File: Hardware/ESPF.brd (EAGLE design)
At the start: 30 x 22 mm, 25 parts, among them IC1 CP2102N-A01-GQFN24, J1 USB-C-16P-16P, J2 ESPFLASH-1X6-2.54-PINS-RA, Q1 MMDT3904

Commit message: Wurth_Connectors_WR-USB
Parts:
- added J3: 629722000214, Wurth_Connectors_WR-USB:629722000214
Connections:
- removed net VIN: F1.1, J1.A4B9, J1.A9B4
- new net +5V: J3.A4, J3.A9, J3.B4, J3.B9
- net 5V: now also F1.1, J1.A4B9, J1.A9B4
- net D+: now also J3.A7, J3.B7
- net D-: now also J3.A6, J3.B6
- net GND: now also J3.A1, J3.A12, J3.B1, J3.B12
- net N$10: now also J3.A5
- net N$9: now also J3.B5
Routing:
- net VIN: track 18.5 -> 0.00 mm, vias 2 -> 0
- net 5V: track 25.9 -> 44.5 mm, vias 2 -> 4
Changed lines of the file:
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@@
 </layers>
 <board>
-<fusionsync huburn="a.cGVyc29uYWw6dWUyZDliZmNi" projecturn="a.cGVyc29uYWw6dWUyZDliZmNiIzIwMTkwNjE5MTk5NjgzNjgx" f3durn="urn:adsk.wipprod:dm.lineage:swBH170zRHaojB2h5Vblyg" pcbguid="" lastpulledtime="" lastsyncedchangeguid="8f27d1c3-c2be-d358-18db-d89d43a70d9e" latestrevisionid="aa437058-996b-450f-af31-aa14738bf436" lastsyncedrevisionid="aa437058-996b-450f-af31-aa14738bf436" lastboardhashguid="c4cc12bd-3535-9094-fdde-aad7011a1909" lastpushedtime="2021-05-06T07:46:15Z" linktopcb3d="true"/>
+<fusionsync huburn="a.cGVyc29uYWw6dWUyZDliZmNi" projecturn="a.cGVyc29uYWw6dWUyZDliZmNiIzIwMTkwNjE5MTk5NjgzNjgx" f3durn="urn:adsk.wipprod:dm.lineage:swBH170zRHaojB2h5Vblyg" pcbguid="" lastpulledtime="" lastsyncedchangeguid="8f27d1c3-c2be-d358-18db-d89d43a70d9e" latestrevisionid="aa437058-996b-450f-af31-aa14738bf436" lastsyncedrevisionid="aa437058-996b-450f-af31-aa14738bf436" lastboardhashguid="c4cc12bd-3535-9094-fdde-aad7011a1909" lastpushedtime="2021-05-06T07:46:15Z" linktopcb3d="false"/>
 <plain>
 <text x="10.25" y="20.55" size="1.2" layer="21" font="vector" ratio="18">superhouse.tv/espf</text>
@@
 <attribute name="VALUE" x="23.284" y="4.6348" size="0.8128" layer="27" font="vector"/>
 </element>
+<element name="J3" library="Wurth_Connectors_WR-USB" library_urn="urn:adsk.eagle:library:16513831" package="629722000214" package3d_urn="urn:adsk.eagle:package:32827710/4" value="629722000214" x="2" y="12" smashed="yes" rot="R270">
+<attribute name="APPLICATION" value="USB 2.0" x="2" y="12" size="1.778" layer="27" rot="R270" display="off"/>
+<attribute name="DATASHEET-URL" value="https://www.we-online.com/redexpert/spec/629722000214?ae" x="2" y="12" size="1.778" layer="27" rot="R270" display="off"/>
+<attribute name="GERDER" value="Receptacle" x="2" y="12" size="1.778" layer="27" rot="R270" display="off"/>
+<attribute name="INTERFACE-TYPE" value="Type C" x="2" y="12" size="1.778" layer="27" rot="R270" display="off"/>
+<attribute name="IR" value="5A" x="2" y="12" size="1.778" layer="27" rot="R270" display="off"/>
+<attribute name="MOUNT" value="SMT" x="2" y="12" size="1.778" layer="27" rot="R270" display="off"/>
+<attribute name="NAME" x="8.18" y="12" size="1.27" layer="25" rot="R270" align="bottom-center"/>
+<attribute name="PACKAGING" value="Tape and Reel" x="2" y="12" size="1.778" layer="27" rot="R270" display="off"/>
+<attribute name="PART-NUMBER" value="629722000214" x="2" y="12" size="1.778" layer="27" rot="R270" display="off"/>
+<attribute name="PINS" value=" 16 " x="2" y="12" size="1.778" layer="27" rot="R270" display="off"/>
+<attribute name="TYPE" value="Horizontal" x="2" y="12" size="1.778" layer="27" rot="R270" display="off"/>
+<attribute name="VALUE" x="-2.82" y="12" size="1.27" layer="27" rot="R270" align="bottom-center"/>
+<attribute name="WORKING-VOLTAGE" value="20V(AC)" x="2" y="12" size="1.778" layer="27" rot="R270" display="off"/>
+</element>
 </elements>
 <signals>
@@
 <wire x1="11.75" y1="17.488" x2="13.738" y2="15.5" width="0.508" layer="1"/>
 <wire x1="13.738" y1="15.5" x2="14.5" y2="15.5" width="0.508" layer="1"/>
+<contactref element="F1" pad="1"/>
+<contactref element="J1" pad="A4B9"/>
+<contactref element="J1" pad="A9B4"/>
+<wire x1="7.095" y1="9.55" x2="8.19565625" y2="9.55" width="0.4064" layer="1"/>
+<wire x1="9" y1="8.74565625" x2="9" y2="8.5" width="0.4064" layer="1"/>
+<wire x1="8.19565625" y1="9.55" x2="9" y2="8.74565625" width="0.4064" layer="1"/>
+<via x="9" y="8.5" extent="1-16" drill="0.5"/>
+<wire x1="9" y1="8.5" x2="8.5" y2="9" width="0.4064" layer="16"/>
+<wire x1="8.5" y1="14" x2="9" y2="14.5" width="0.4064" layer="16"/>
+<via x="9" y="14.5" extent="1-16" drill="0.5"/>
+<wire x1="9" y1="14.5" x2="8.95" y2="14.45" width="0.4064" layer="1"/>
+<wire x1="8.95" y1="14.45" x2="7.095" y2="14.45" width="0.4064" layer="1"/>
+<wire x1="8.5" y1="9" x2="8.5" y2="14" width="0.4064" layer="16"/>
+<wire x1="9" y1="14.5" x2="9" y2="15.5" width="0.508" layer="1"/>
+<wire x1="4.8" y1="18.2" x2="4.55" y2="18.45" width="0.4064" layer="1"/>
+<wire x1="9" y1="15.5" x2="6.3" y2="18.2" width="0.508" layer="1"/>
+<wire x1="6.3" y1="18.2" x2="4.8" y2="18.2" width="0.508" layer="1"/>
+<wire x1="4.55" y1="18.45" x2="4.55" y2="19.5" width="0.4064" layer="1"/>
+<wire x1="4.55" y1="19.5" x2="8.45" y2="19.5" width="0" layer="19" extent="1-1"/>
 </signal>
 <signal name="GND">
@@
 <wire x1="7.095" y1="8.095" x2="6.68" y2="7.68" width="0.508" layer="1"/>
 <contactref element="C3" pad="2"/>
+<contactref element="J3" pad="A1"/>
+<contactref element="J3" pad="B12"/>
+<contactref element="J3" pad="A12"/>
+<contactref element="J3" pad="B1"/>
 <wire x1="16.75" y1="11.75" x2="17" y2="11" width="0" layer="19" extent="1-1"/>
+<wire x1="6.745" y1="8.65" x2="7.095" y2="8.775" width="0" layer="19" extent="1-1"/>
+<wire x1="7.095" y1="15.225" x2="11" y2="14.262" width="0" layer="19" extent="1-1"/>
+<wire x1="6.745" y1="15.35" x2="7.095" y2="15.225" width="0" layer="19" extent="1-1"/>
+<wire x1="2" y1="16.32" x2="6.18" y2="16.32" width="0" layer="19" extent="1-1"/>
+<wire x1="2" y1="7.68" x2="6.18" y2="7.68" width="0" layer="19" extent="1-1"/>
 </signal>
 <signal name="D-">
@@
 <wire x1="15.1" y1="10.75" x2="13" y2="10.75" width="0.254" layer="1"/>
 <wire x1="13" y1="10.75" x2="12.5" y2="10.25" width="0.254" layer="1"/>
+<contactref element="J3" pad="B6"/>
+<contactref element="J3" pad="A6"/>
+<wire x1="6.745" y1="11.25" x2="7.095" y2="11.75" width="0" layer="19" extent="1-1"/>
+<wire x1="6.745" y1="12.25" x2="7.095" y2="12.75" width="0" layer="19" extent="1-1"/>
 </signal>
 <signal name="D+">
@@
 <wire x1="7.095" y1="11.25" x2="12" y2="11.25" width="0.254" layer="1"/>
 <wire x1="12" y1="11.25" x2="12.5" y2="11.75" width="0.254" layer="1"/>
+<contactref element="J3" pad="A7"/>
+<contactref element="J3" pad="B7"/>
+<wire x1="7.095" y1="12.25" x2="6.745" y2="12.75" width="0" layer="19" extent="1-1"/>
+<wire x1="6.745" y1="11.75" x2="7.095" y2="12.25" width="0" layer="19" extent="1-1"/>
 </signal>
 <signal name="3.3V">
@@
 <wire x1="18.25" y1="12.9" x2="18.9" y2="12.9" width="0.254" layer="1"/>
 </signal>
-<signal name="VIN">
-<contactref element="F1" pad="1"/>
-<contactref element="J1" pad="A4B9"/>
-<contactref element="J1" pad="A9B4"/>
-<wire x1="7.095" y1="9.55" x2="8.19565625" y2="9.55" width="0.4064" layer="1"/>
-<wire x1="9" y1="8.74565625" x2="9" y2="8.5" width="0.4064" layer="1"/>
-<wire x1="8.19565625" y1="9.55" x2="9" y2="8.74565625" width="0.4064" layer="1"/>
-<via x="9" y="8.5" extent="1-16" drill="0.5"/>
-<wire x1="9" y1="8.5" x2="8.5" y2="9" width="0.4064" layer="16"/>
-<wire x1="8.5" y1="14" x2="9" y2="14.5" width="0.4064" layer="16"/>
-<via x="9" y="14.5" extent="1-16" drill="0.5"/>
-<wire x1="9" y1="14.5" x2="8.95" y2="14.45" width="0.4064" layer="1"/>
-<wire x1="8.95" y1="14.45" x2="7.095" y2="14.45" width="0.4064" layer="1"/>
-<wire x1="8.5" y1="9" x2="8.5" y2="14" width="0.4064" layer="16"/>
-<wire x1="9" y1="14.5" x2="9" y2="15.5" width="0.508" layer="1"/>
-<wire x1="4.8" y1="18.2" x2="4.55" y2="18.45" width="0.4064" layer="1"/>
-<wire x1="9" y1="15.5" x2="6.3" y2="18.2" width="0.508" layer="1"/>
-<wire x1="6.3" y1="18.2" x2="4.8" y2="18.2" width="0.508" layer="1"/>
-<wire x1="4.55" y1="18.45" x2="4.55" y2="19.5" width="0.4064" layer="1"/>
-</signal>
 <signal name="N$6">
 <contactref element="R7" pad="1"/>
@@
 <wire x1="9.238" y1="9.262" x2="11" y2="9.262" width="0.254" layer="1"/>
 <wire x1="8.25" y1="10.25" x2="9.238" y2="9.262" width="0.254" layer="1"/>
+<contactref element="J3" pad="B5"/>
+<wire x1="6.745" y1="10.25" x2="7.095" y2="10.25" width="0" layer="19" extent="1-1"/>
 </signal>
 <signal name="N$10">
@@
 <wire x1="7.095" y1="13.25" x2="10.488" y2="13.25" width="0.254" layer="1"/>
 <wire x1="10.488" y1="13.25" x2="11" y2="12.738" width="0.254" layer="1"/>
+<contactref element="J3" pad="A5"/>
+<wire x1="6.745" y1="13.25" x2="7.095" y2="13.25" width="0" layer="19" extent="1-1"/>
+</signal>
+<signal name="+5V">
+<contactref element="J3" pad="A4"/>
+<contactref element="J3" pad="A9"/>
+<contactref element="J3" pad="B4"/>
+<contactref element="J3" pad="B9"/>
+<wire x1="6.745" y1="14.25" x2="6.745" y2="14.55" width="0" layer="19" extent="1-1"/>
+<wire x1="6.745" y1="9.75" x2="6.745" y2="14.25" width="0" layer="19" extent="1-1"/>
+<wire x1="6.745" y1="9.45" x2="6.745" y2="9.75" width="0" layer="19" extent="1-1"/>
 </signal>
 </signals>

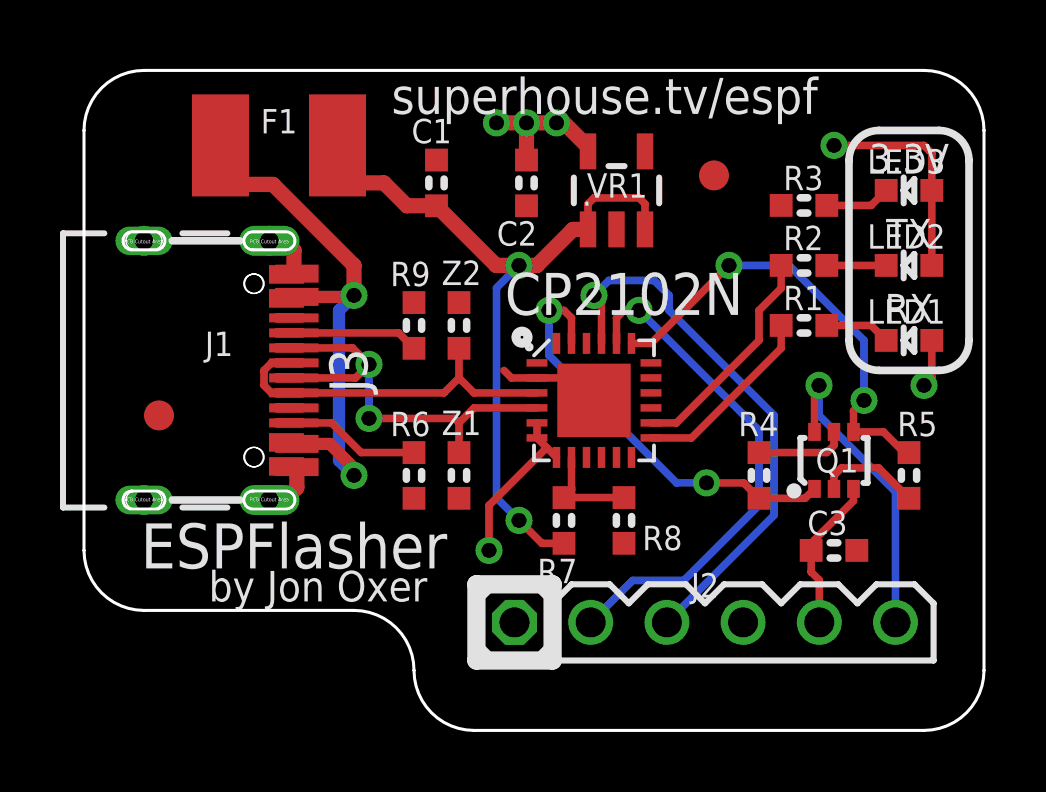
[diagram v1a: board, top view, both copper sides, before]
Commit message: With Würht Connectors.
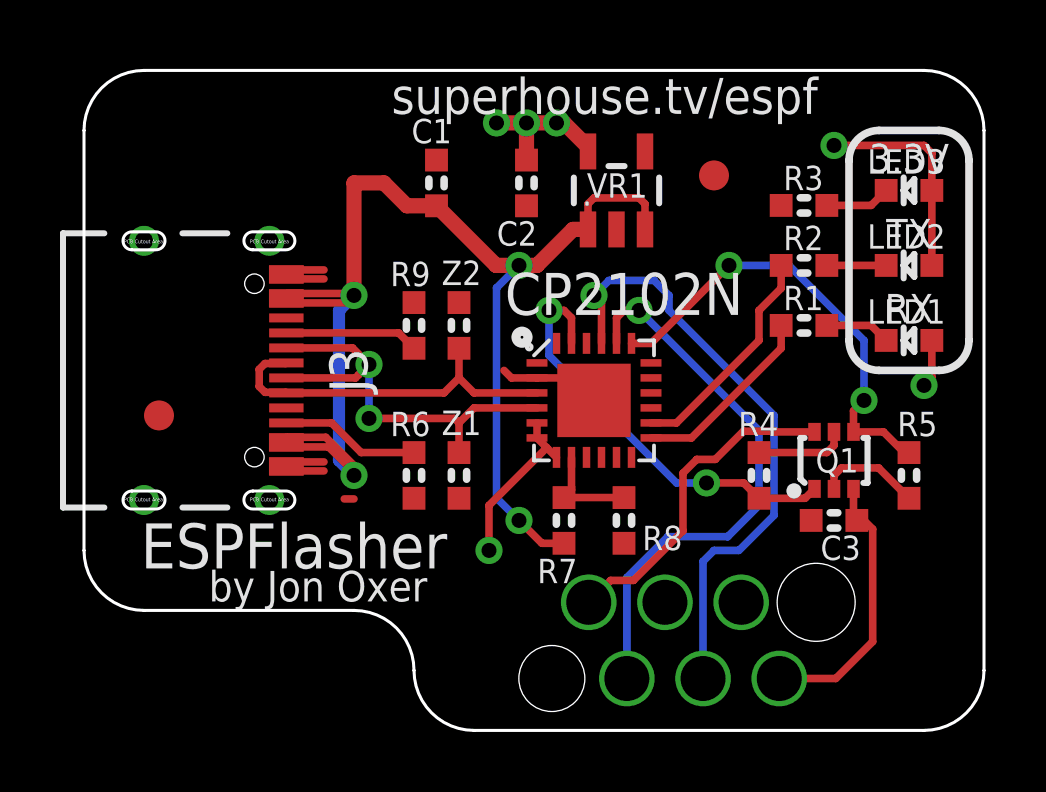
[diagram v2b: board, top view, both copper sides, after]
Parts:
- removed F1: 500mA 1812 PTC, SuperHouse-Fuses:1812
- removed J2: ESPFLASH-1X6-2.54-PINS-RA, SuperHouse-ESPFlash:1X6-2.54-PINS-RA
- J1: value USB-C-16P-16P -> 490107670612; device SuperHouse-Connectors:USB-C-16P -> Wurth_Connectors_WR-WST:490107670612_DEBUGGING
- moved J1 20.1 mm to (20.0, 3.00), flipped to the bottom, turned to 180 degrees
- moved C3 1.00 mm to (25.0, 7.00), turned to 180 degrees
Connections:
- removed net 3.3V: C2.1, IC1.5, IC1.6, IC1.7, J2.4, LED1.A, LED2.A, LED3.A, VR1.5
- removed net 5V: C1.1, F1.1, F1.2, J1.A4B9, J1.A9B4, R7.2, VR1.1, VR1.3
- new net +3V3: C2.1, IC1.5, IC1.6, IC1.7, J1.2, LED1.A, LED2.A, LED3.A, VR1.5
- net +5V: now also C1.1, R7.2, VR1.1, VR1.3
- net D+: now also J3.A6, J3.B6; no longer J1.A6, J1.B6, J3.A7, J3.B7
- net D-: now also J3.A7, J3.B7; no longer J1.A7, J1.B7, J3.A6, J3.B6
- net EN: now also J1.1; no longer J2.5
- net GND: now also J1.4; no longer J1.A12B1, J1.A1B12, J1.FIX1, J1.FIX2, J1.FIX3, J1.FIX4, J2.1
- net GPIO0: now also J1.6; no longer J2.6
- net N$10: no longer J1.A5
- net N$9: no longer J1.B5
- net RXI: now also J1.5; no longer J2.2
- net TXO: now also J1.3; no longer J2.3
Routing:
- net +5V: track 0.00 -> 44.8 mm, vias 0 -> 4
- net 5V: track 44.5 -> 0.00 mm, vias 4 -> 0
- net 3.3V: track 19.1 -> 0.00 mm, vias 6 -> 0
- net +3V3: track 0.00 -> 19.1 mm, vias 0 -> 6
- net EN: track 5.15 -> 9.12 mm
- net GND: track 6.39 -> 8.76 mm
- net TXO: track 18.4 -> 20.3 mm
- net RXI: track 17.1 -> 18.6 mm
- net D-: track 13.9 -> 14.6 mm
- net GPIO0: track 10.6 -> 11.0 mm, vias 1 -> 0
- added copper zone on layer 16, net +3V3
- removed copper zone on layer 16, net 3.3V
